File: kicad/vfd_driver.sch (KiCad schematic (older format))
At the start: 40 parts, among them CON1 AVR-ISP-6, J1 PWR, J6 MH, J7 MH, J8 MH, J9 MH, U1 ATTINY2313-20SU, U10 74HC595, U11 74HC595, U12 74HC595, U13 74HC595, U14 ULN2803A, U15 ULN2803A, U16 ULN2003, U17 ULN2003, U18 LM1117-3.3, U2 74HC595, U3 74HC595, U4 74HC595, U5 74HC595, U6 ULN2803A, U7 ULN2003, U8 ULN2003, U9 ULN2003

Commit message: routing
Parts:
- removed R13: 0, Resistors_SMD:R_1206, symbol R_Small
- removed U10, U11, U12, U13, U2, U3, U4, U5: 74HC595, Housings_SOIC:SOIC-16_3.9x9.9mm_Pitch1.27mm, symbol 74HC595
- removed U14, U15, U6: ULN2803A, Housings_SOIC:SOIC-18W_7.5x11.6mm_Pitch1.27mm, symbol ULN2803A
- removed U16, U17, U7, U8, U9: ULN2003, Housings_SOIC:SOIC-16_3.9x9.9mm_Pitch1.27mm, symbol ULN2003
- renumbered C3 to C2, C4 to C3, C2 to C4, D2 to D1, J7 to J2, J8 to J3, J6 to J4, J9 to J5, R1 to R3, R5 to R4, U18 to U5, U1 to U6
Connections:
- net RCLK_1 is gone; now on net SRCLK: U6.3 ((TXD)PD1)
- net RCLK_2 is gone; now on net SRCLR: U6.2 ((RXD)PD0)
- net RCLK_4 is gone; now on net RCLK_0: U6.8 ((T0)PD4)
- net RCLK_0: now also R8.1; no longer U6.4 (PA1(XTAL2))
- net RCLK_7: now also R9.1
- net SRCLK: no longer U6.14 ((PCINT2/OC0A)PB2)
- net SRCLR: no longer U6.13 ((PCINT1/AIN1)PB1)
- net Sheet5A13BBBF/SER: now reaches R15.1
- net Sheet5A11F95F/RCLK: now reaches R11.1
- net Sheet5A11F95F/RCLK: now also R10.2
- net Sheet5A13BBCF/SER: now reaches R14.1
- net Sheet5A12BB8F/RCLK: now reaches R10.1
- net Sheet5A12BB8F/RCLK: now also R9.2
- net Sheet5A12BB9F/RCLK: now reaches R12.1
- net Sheet5A12BB9F/RCLK: now also R11.2
- net RCLK_3: no longer names the net of U6.9 ((OC0B/T1)PD5)
- net RCLK_5 renamed SER_POS
- net RCLK_6 renamed SER_DAT
- removed net SER: R10.2, R11.2, R12.2, R14.2, R15.2, R8.2, R9.2, U6.12 ((PCINT0/AIN0)PB0)
- new net Sheet5A12BBAF/RCLK: R12.2
- new net Sheet5A13BBAF/RCLK: R8.2
- new net Sheet5A13BBAF/SER_OUT: R14.2
- new net Sheet5A13BBCF/SER_OUT: R15.2
- no-connect marks 13 -> 10
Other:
- moved on the sheet: C1, C2, C3, C4, C5, CON1, D1, J1, J2, J3, J4, J5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

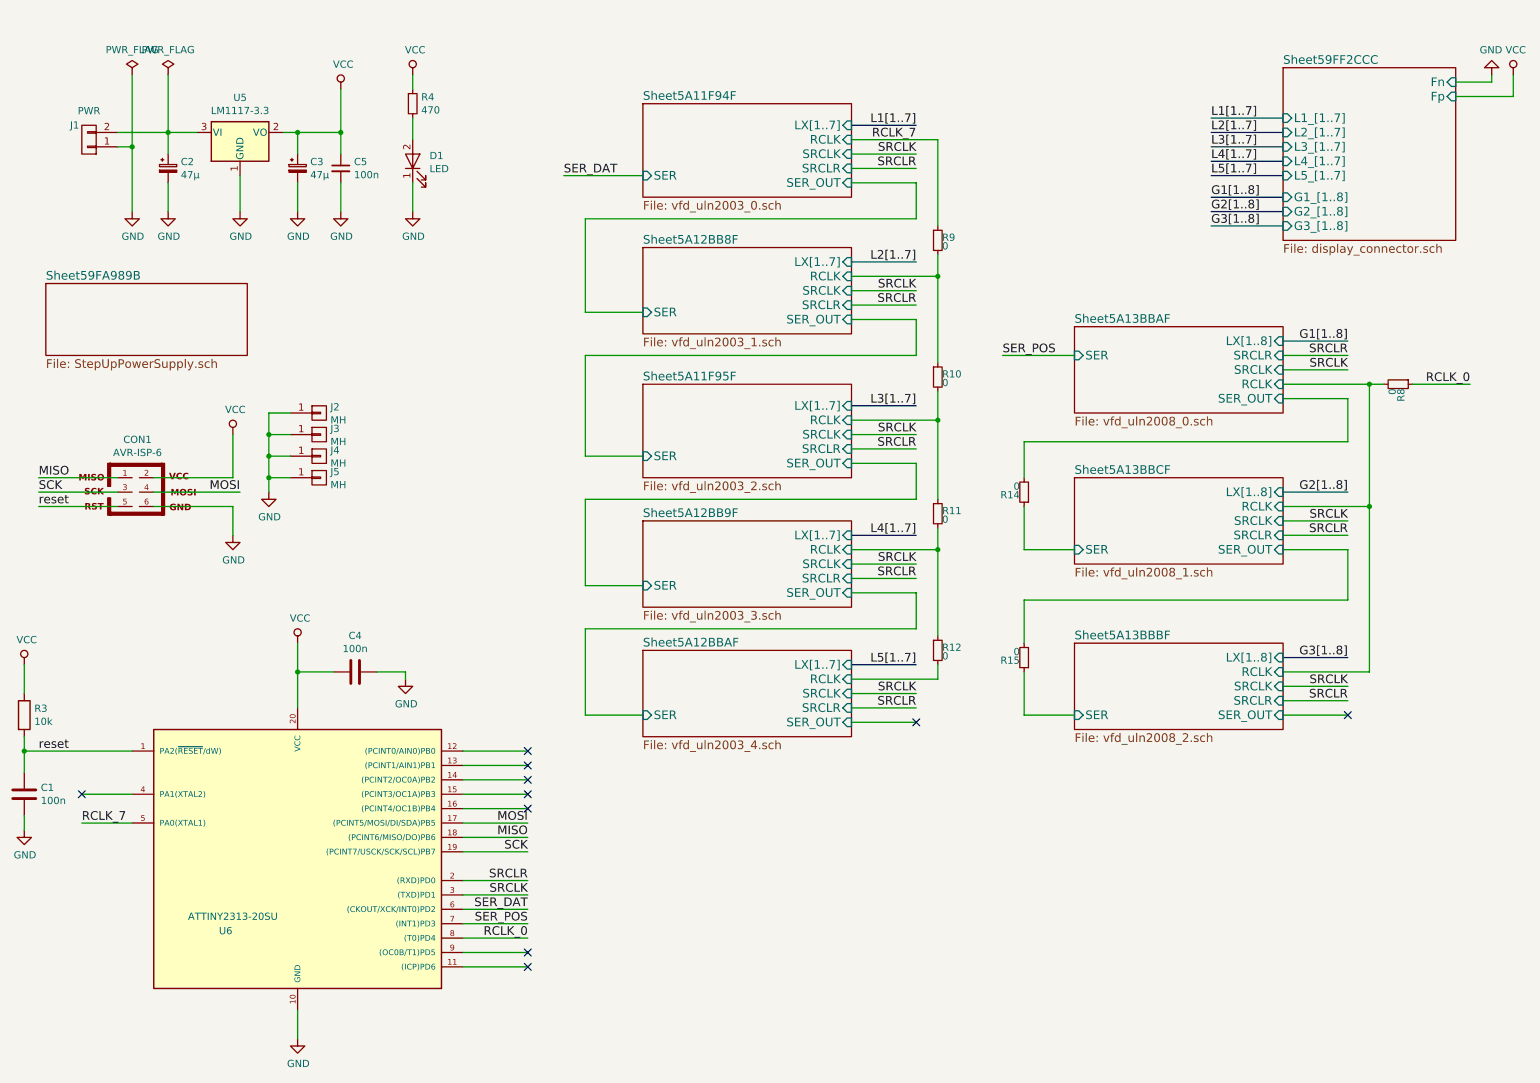
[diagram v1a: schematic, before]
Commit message: Not working need high side driver
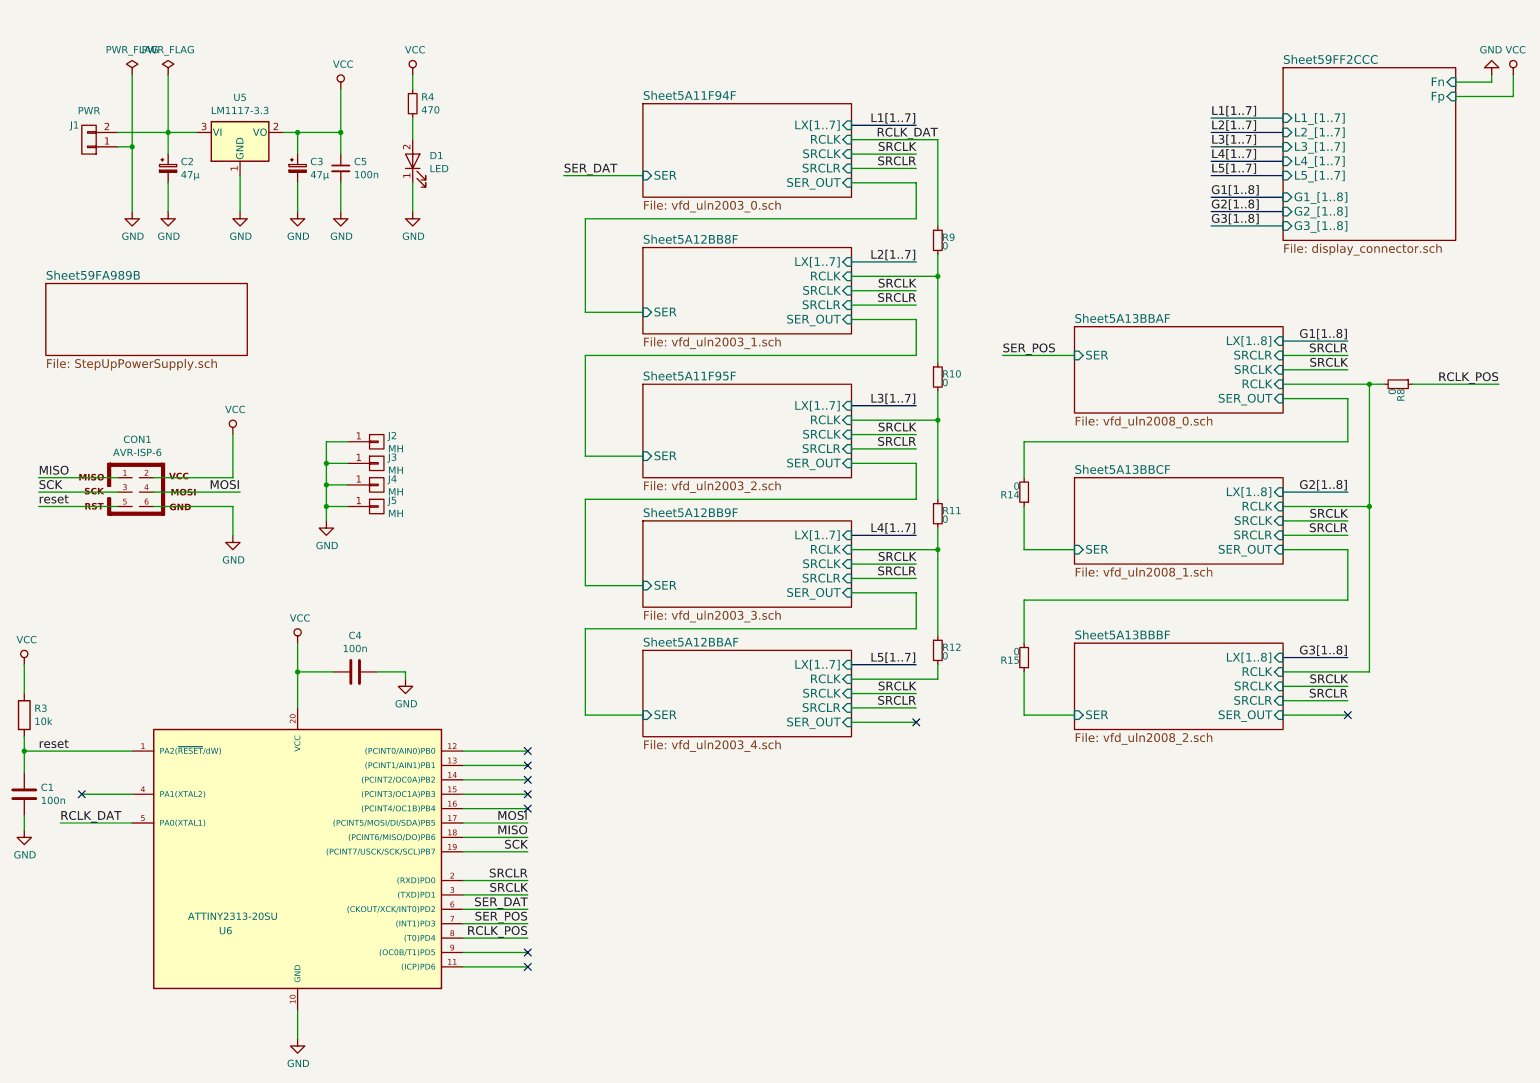
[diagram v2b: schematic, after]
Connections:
- net RCLK_0 renamed RCLK_POS
- net RCLK_7 renamed RCLK_DAT
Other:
- moved on the sheet: J2, J3, J4, J5
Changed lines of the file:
@@
 L CONN_01X01 J4
 U 1 1 59D8A174
-P 2700 3500
-F 0 "J4" H 2778 3541 50  0000 L CNN
-F 1 "MH" H 2778 3450 50  0000 L CNN
-F 2 "Mounting_Holes:MountingHole_3.2mm_M3_DIN965_Pad" H 2700 3500 50  0001 C CNN
-F 3 "" H 2700 3500 50  0001 C CNN
-	1    2700 3500
+P 3100 3700
+F 0 "J4" H 3178 3741 50  0000 L CNN
+F 1 "MH" H 3178 3650 50  0000 L CNN
+F 2 "Mounting_Holes:MountingHole_3.2mm_M3_DIN965_Pad" H 3100 3700 50  0001 C CNN
+F 3 "" H 3100 3700 50  0001 C CNN
+	1    3100 3700
 	1    0    0    -1
 $EndComp
@@
 L GND #PWR8
 U 1 1 59D8A463
-P 2350 3750
-F 0 "#PWR8" H 2350 3500 50  0001 C CNN
-F 1 "GND" H 2355 3577 50  0000 C CNN
-F 2 "" H 2350 3750 50  0001 C CNN
-F 3 "" H 2350 3750 50  0001 C CNN
-	1    2350 3750
+P 2750 3950
+F 0 "#PWR8" H 2750 3700 50  0001 C CNN
+F 1 "GND" H 2755 3777 50  0000 C CNN
+F 2 "" H 2750 3950 50  0001 C CNN
+F 3 "" H 2750 3950 50  0001 C CNN
+	1    2750 3950
 	1    0    0    -1
 $EndComp
@@
 L CONN_01X01 J3
 U 1 1 59D8A8E1
-P 2700 3350
-F 0 "J3" H 2778 3391 50  0000 L CNN
-F 1 "MH" H 2778 3300 50  0000 L CNN
-F 2 "Mounting_Holes:MountingHole_3.2mm_M3_DIN965_Pad" H 2700 3350 50  0001 C CNN
-F 3 "" H 2700 3350 50  0001 C CNN
-	1    2700 3350
+P 3100 3550
+F 0 "J3" H 3178 3591 50  0000 L CNN
+F 1 "MH" H 3178 3500 50  0000 L CNN
+F 2 "Mounting_Holes:MountingHole_3.2mm_M3_DIN965_Pad" H 3100 3550 50  0001 C CNN
+F 3 "" H 3100 3550 50  0001 C CNN
+	1    3100 3550
 	1    0    0    -1
 $EndComp
@@
 L CONN_01X01 J2
 U 1 1 59D8A925
-P 2700 3200
-F 0 "J2" H 2778 3241 50  0000 L CNN
-F 1 "MH" H 2778 3150 50  0000 L CNN
-F 2 "Mounting_Holes:MountingHole_3.2mm_M3_DIN965_Pad" H 2700 3200 50  0001 C CNN
-F 3 "" H 2700 3200 50  0001 C CNN
-	1    2700 3200
+P 3100 3400
+F 0 "J2" H 3178 3441 50  0000 L CNN
+F 1 "MH" H 3178 3350 50  0000 L CNN
+F 2 "Mounting_Holes:MountingHole_3.2mm_M3_DIN965_Pad" H 3100 3400 50  0001 C CNN
+F 3 "" H 3100 3400 50  0001 C CNN
+	1    3100 3400
 	1    0    0    -1
 $EndComp
@@
 L CONN_01X01 J5
 U 1 1 59D8A96F
-P 2700 3650
-F 0 "J5" H 2778 3691 50  0000 L CNN
-F 1 "MH" H 2778 3600 50  0000 L CNN
-F 2 "Mounting_Holes:MountingHole_3.2mm_M3_DIN965_Pad" H 2700 3650 50  0001 C CNN
-F 3 "" H 2700 3650 50  0001 C CNN
-	1    2700 3650
+P 3100 3850
+F 0 "J5" H 3178 3891 50  0000 L CNN
+F 1 "MH" H 3178 3800 50  0000 L CNN
+F 2 "Mounting_Holes:MountingHole_3.2mm_M3_DIN965_Pad" H 3100 3850 50  0001 C CNN
+F 3 "" H 3100 3850 50  0001 C CNN
+	1    3100 3850
 	1    0    0    -1
 $EndComp
@@
 Text Label 4150 6450 2    60   ~ 0
 SRCLR
-Text Label 1050 6050 0    60   ~ 0
-RCLK_7
+Text Label 900  6050 0    60   ~ 0
+RCLK_DAT
 Text Label 4150 6850 2    60   ~ 0
-RCLK_0
+RCLK_POS
 $Comp
 L LM1117-3.3 U5
@@
 Wire Wire Line
 	1550 3650 2100 3650
-Connection ~ 2350 3350
-Wire Wire Line
-	2500 3200 2350 3200
-Connection ~ 2350 3650
-Wire Wire Line
-	2500 3650 2350 3650
-Connection ~ 2350 3500
-Wire Wire Line
-	2500 3350 2350 3350
-Wire Wire Line
-	2350 3500 2500 3500
-Wire Wire Line
-	2350 3200 2350 3750
+Connection ~ 2750 3550
+Wire Wire Line
+	2900 3400 2750 3400
+Connection ~ 2750 3850
+Wire Wire Line
+	2900 3850 2750 3850
+Connection ~ 2750 3700
+Wire Wire Line
+	2900 3550 2750 3550
+Wire Wire Line
+	2750 3700 2900 3700
+Wire Wire Line
+	2750 3400 2750 3950
 Wire Wire Line
 	3350 1150 3350 1300
@@
 	1400 5850 1050 5850
 Wire Wire Line
-	1050 6050 1400 6050
+	900  6050 1400 6050
 $Sheet
 S 4950 1050 1450 650
@@
 Text Label 6850 1500 2    60   ~ 0
 SRCLR
-Text Label 6850 1300 2    60   ~ 0
-RCLK_7
+Text Label 7000 1300 2    60   ~ 0
+RCLK_DAT
 NoConn ~ 4150 5950
 NoConn ~ 4150 7050
@@
 Wire Wire Line
 	9850 3100 9400 3100
-Text Label 10700 3000 2    60   ~ 0
-RCLK_0
+Text Label 10900 3000 2    60   ~ 0
+RCLK_POS
 Text Label 9850 2800 2    60   ~ 0
 SRCLR
@@
 Connection ~ 10000 3000
 Wire Wire Line
-	10700 3000 10300 3000
+	10300 3000 10900 3000
 Wire Wire Line
 	10000 3000 10000 5000
